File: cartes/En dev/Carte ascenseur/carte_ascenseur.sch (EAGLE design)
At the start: 21 parts, among them U1 MCP2551, U2 ADUM1250ARZ, U3 ADUM1400ARWZ

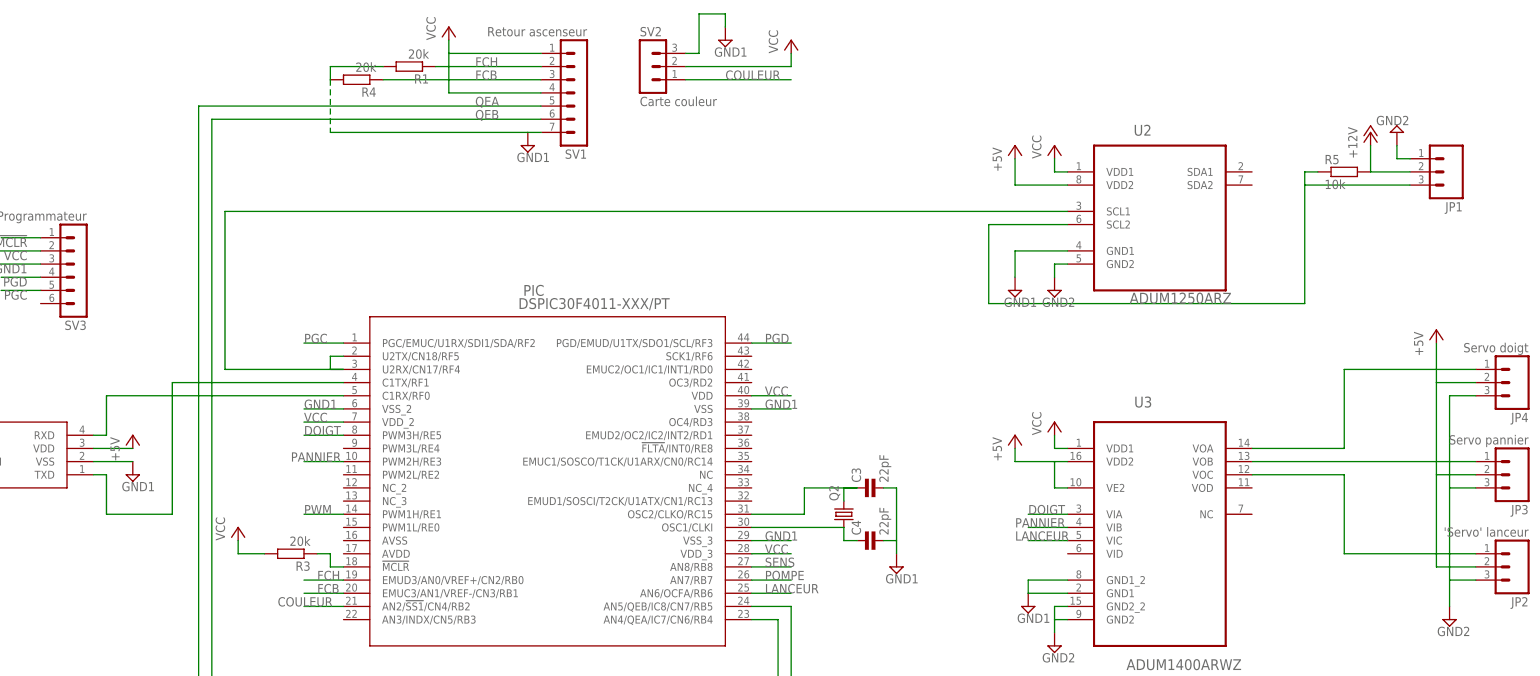
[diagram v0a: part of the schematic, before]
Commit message: Correction de la carte ascenseur
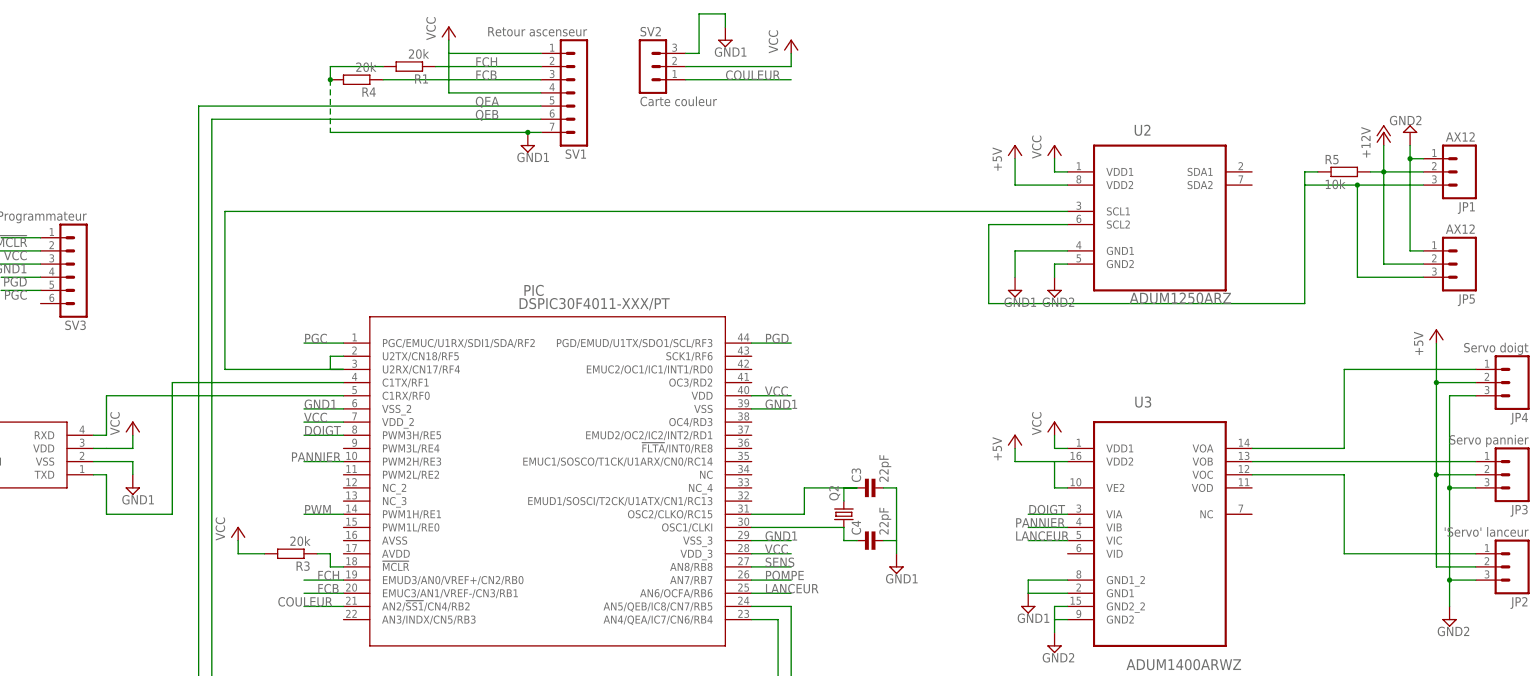
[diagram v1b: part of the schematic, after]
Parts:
- added JP5: AX12, SparkFun-Connectors:M03POLAR
- JP1: value (none) -> AX12
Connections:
- net +12V: now also JP5.2
- net +5V: no longer U1.VDD
- net GND2: now also JP5.1
- net N$16: now also JP5.3
- net VCC: now also U1.VDD
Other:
- moved on the sheet: JP1
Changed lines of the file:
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@@
 <setting verticaltext="up"/>
 </settings>
-<grid distance="0.1" unitdist="inch" unit="inch" style="dots" multiple="1" display="yes" altdistance="0.01" altunitdist="inch" altunit="inch"/>
+<grid distance="0.1" unitdist="inch" unit="inch" style="lines" multiple="1" display="no" altdistance="0.01" altunitdist="inch" altunit="inch"/>
 <layers>
 <layer number="1" name="Top" color="4" fill="1" visible="no" active="no"/>
@@
 <part name="SUPPLY2" library="supply2" deviceset="GND1" device=""/>
 <part name="SUPPLY4" library="supply2" deviceset="GND2" device=""/>
-<part name="P+3" library="supply1" deviceset="+5V" device=""/>
 <part name="SUPPLY6" library="supply2" deviceset="GND1" device=""/>
 <part name="R2" library="rcl" deviceset="R-EU_" device="M0805" value="4,7k"/>
@@
 <part name="P+9" library="supply1" deviceset="VCC" device=""/>
 <part name="SUPPLY11" library="supply2" deviceset="GND1" device=""/>
-<part name="JP1" library="SparkFun-Connectors" deviceset="M03" device="POLAR"/>
+<part name="JP1" library="SparkFun-Connectors" deviceset="M03" device="POLAR" value="AX12"/>
 <part name="R5" library="rcl" deviceset="R-EU_" device="M0805" value="10k"/>
 <part name="P+12" library="supply1" deviceset="+12V" device=""/>
@@
 <part name="R1" library="rcl" deviceset="R-EU_" device="M0805" value="20k"/>
 <part name="R4" library="rcl" deviceset="R-EU_" device="M0805" value="20k"/>
+<part name="JP5" library="SparkFun-Connectors" deviceset="M03" device="POLAR" value="AX12"/>
+<part name="P+3" library="supply1" deviceset="VCC" device=""/>
 </parts>
 <sheets>
@@
 <instance part="SUPPLY2" gate="G$1" x="-35.56" y="88.9"/>
 <instance part="SUPPLY4" gate="G$1" x="177.8" y="17.78"/>
-<instance part="P+3" gate="1" x="0" y="58.42"/>
-<instance part="SUPPLY6" gate="G$1" x="0" y="50.8"/>
+<instance part="SUPPLY6" gate="G$1" x="0" y="48.26"/>
 <instance part="R2" gate="G$1" x="-40.64" y="43.18" rot="R90"/>
 <instance part="SUPPLY7" gate="G$1" x="-40.64" y="33.02"/>
@@
 <instance part="P+9" gate="VCC" x="127" y="134.62"/>
 <instance part="SUPPLY11" gate="G$1" x="114.3" y="134.62"/>
-<instance part="JP1" gate="G$1" x="254" y="109.22" rot="R180"/>
+<instance part="JP1" gate="G$1" x="256.54" y="109.22" rot="R180"/>
 <instance part="R5" gate="G$1" x="233.68" y="109.22"/>
-<instance part="P+12" gate="1" x="238.76" y="116.84"/>
-<instance part="SUPPLY13" gate="G$1" x="243.84" y="116.84" rot="R180"/>
+<instance part="P+12" gate="1" x="241.3" y="116.84"/>
+<instance part="SUPPLY13" gate="G$1" x="246.38" y="116.84" rot="R180"/>
 <instance part="P+11" gate="VCC" x="177.8" y="114.3"/>
 <instance part="SUPPLY14" gate="G$1" x="170.18" y="86.36"/>
@@
 <instance part="R1" gate="G$1" x="53.34" y="129.54" rot="R180"/>
 <instance part="R4" gate="G$1" x="43.18" y="127" rot="R180"/>
+<instance part="JP5" gate="G$1" x="256.54" y="91.44" rot="R180"/>
+<instance part="P+3" gate="VCC" x="0" y="60.96"/>
 </instances>
 <busses>
@@
 </net>
 <net name="+5V" class="0">
-<segment>
-<pinref part="U1" gate="G$1" pin="VDD"/>
-<wire x1="-7.62" y1="55.88" x2="0" y2="55.88" width="0.1524" layer="91"/>
-<pinref part="P+3" gate="1" pin="+5V"/>
-</segment>
 <segment>
 <pinref part="P+8" gate="1" pin="+5V"/>
@@
 <wire x1="259.08" y1="68.58" x2="251.46" y2="68.58" width="0.1524" layer="91"/>
 <pinref part="P+10" gate="1" pin="+5V"/>
+<junction x="251.46" y="68.58"/>
+<junction x="251.46" y="50.8"/>
 </segment>
 </net>
@@
 <wire x1="119.38" y1="38.1" x2="127" y2="38.1" width="0.1524" layer="91"/>
 <label x="121.92" y="38.1" size="1.778" layer="95"/>
-</segment>
-<segment>
-<pinref part="U1" gate="G$1" pin="VSS"/>
-<wire x1="-7.62" y1="53.34" x2="0" y2="53.34" width="0.1524" layer="91"/>
-<pinref part="SUPPLY6" gate="G$1" pin="GND1"/>
 </segment>
 <segment>
@@
 <wire x1="38.1" y1="127" x2="38.1" y2="116.84" width="0.1524" layer="91" style="longdash"/>
 <wire x1="38.1" y1="116.84" x2="76.2" y2="116.84" width="0.1524" layer="91"/>
+<junction x="38.1" y="127"/>
+<junction x="76.2" y="116.84"/>
 </segment>
 <segment>
@@
 <pinref part="SUPPLY5" gate="G$1" pin="GND1"/>
 </segment>
+<segment>
+<pinref part="U1" gate="G$1" pin="VSS"/>
+<pinref part="SUPPLY6" gate="G$1" pin="GND1"/>
+<wire x1="-7.62" y1="53.34" x2="0" y2="53.34" width="0.1524" layer="91"/>
+<wire x1="0" y1="53.34" x2="0" y2="50.8" width="0.1524" layer="91"/>
+</segment>
 </net>
 <net name="GND2" class="0">
@@
 <segment>
 <pinref part="JP1" gate="G$1" pin="1"/>
-<wire x1="246.38" y1="111.76" x2="243.84" y2="111.76" width="0.1524" layer="91"/>
-<wire x1="243.84" y1="111.76" x2="243.84" y2="114.3" width="0.1524" layer="91"/>
+<wire x1="248.92" y1="111.76" x2="246.38" y2="111.76" width="0.1524" layer="91"/>
+<wire x1="246.38" y1="111.76" x2="246.38" y2="114.3" width="0.1524" layer="91"/>
 <pinref part="SUPPLY13" gate="G$1" pin="GND2"/>
+<pinref part="JP5" gate="G$1" pin="1"/>
+<wire x1="246.38" y1="111.76" x2="246.38" y2="93.98" width="0.1524" layer="91"/>
+<wire x1="246.38" y1="93.98" x2="248.92" y2="93.98" width="0.1524" layer="91"/>
+<junction x="246.38" y="111.76"/>
 </segment>
 <segment>
@@
 <pinref part="JP3" gate="G$1" pin="3"/>
 <wire x1="259.08" y1="48.26" x2="254" y2="48.26" width="0.1524" layer="91"/>
+<junction x="254" y="48.26"/>
+<junction x="254" y="30.48"/>
 </segment>
 </net>
@@
 </segment>
 </net>
-<net name="+12V" class="0">
-<segment>
-<pinref part="JP1" gate="G$1" pin="2"/>
-<pinref part="R5" gate="G$1" pin="2"/>
-<wire x1="246.38" y1="109.22" x2="238.76" y2="109.22" width="0.1524" layer="91"/>
-<wire x1="238.76" y1="109.22" x2="238.76" y2="114.3" width="0.1524" layer="91"/>
-<pinref part="P+12" gate="1" pin="+12V"/>
-</segment>
-</net>
 <net name="VCC" class="0">
 <segment>
@@
 <wire x1="71.12" y1="-25.4" x2="71.12" y2="-22.86" width="0.1524" layer="91"/>
 </segment>
+<segment>
+<pinref part="P+3" gate="VCC" pin="VCC"/>
+<wire x1="-5.08" y1="55.88" x2="0" y2="55.88" width="0.1524" layer="91"/>
+<wire x1="0" y1="58.42" x2="0" y2="55.88" width="0.1524" layer="91"/>
+<pinref part="U1" gate="G$1" pin="VDD"/>
+<wire x1="-5.08" y1="55.88" x2="-7.62" y2="55.88" width="0.1524" layer="91"/>
+</segment>
 </net>
 <net name="POMPE" class="0">
@@
 <wire x1="226.06" y1="109.22" x2="226.06" y2="106.68" width="0.1524" layer="91"/>
 <pinref part="JP1" gate="G$1" pin="3"/>
-<wire x1="226.06" y1="106.68" x2="246.38" y2="106.68" width="0.1524" layer="91"/>
+<wire x1="226.06" y1="106.68" x2="236.22" y2="106.68" width="0.1524" layer="91"/>
 <pinref part="U2" gate="A" pin="SCL2"/>
+<wire x1="236.22" y1="106.68" x2="248.92" y2="106.68" width="0.1524" layer="91"/>
 <wire x1="180.34" y1="99.06" x2="165.1" y2="99.06" width="0.1524" layer="91"/>
 <wire x1="165.1" y1="99.06" x2="165.1" y2="83.82" width="0.1524" layer="91"/>
 <wire x1="165.1" y1="83.82" x2="226.06" y2="83.82" width="0.1524" layer="91"/>
 <wire x1="226.06" y1="83.82" x2="226.06" y2="106.68" width="0.1524" layer="91"/>
+<wire x1="236.22" y1="106.68" x2="236.22" y2="88.9" width="0.1524" layer="91"/>
+<wire x1="236.22" y1="88.9" x2="248.92" y2="88.9" width="0.1524" layer="91"/>
+<pinref part="JP5" gate="G$1" pin="3"/>
+<junction x="236.22" y="106.68"/>
 </segment>
 </net>
@@
 </segment>
 </net>
+<net name="+12V" class="0">
+<segment>
+<pinref part="JP5" gate="G$1" pin="2"/>
+<wire x1="241.3" y1="91.44" x2="248.92" y2="91.44" width="0.1524" layer="91"/>
+<pinref part="P+12" gate="1" pin="+12V"/>
+<wire x1="241.3" y1="114.3" x2="241.3" y2="109.22" width="0.1524" layer="91"/>
+<pinref part="JP1" gate="G$1" pin="2"/>
+<pinref part="R5" gate="G$1" pin="2"/>
+<wire x1="241.3" y1="109.22" x2="241.3" y2="91.44" width="0.1524" layer="91"/>
+<wire x1="248.92" y1="109.22" x2="241.3" y2="109.22" width="0.1524" layer="91"/>
+<junction x="241.3" y="109.22"/>
+<wire x1="241.3" y1="109.22" x2="238.76" y2="109.22" width="0.1524" layer="91"/>
+</segment>
+</net>
